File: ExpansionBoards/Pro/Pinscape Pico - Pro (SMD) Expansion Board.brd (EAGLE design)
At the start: 170.6 x 108 mm, 213 parts, among them IC1 UCC27523D, IC10 UCC27523D, IC11 UCC27523D, IC12 UCC27523D, IC13 UCC27523D, IC14 UCC27523D, IC15 TLC59116FIRHBR, IC16 TLC59116FIRHBR, IC17 TLC59116FIRHBR, IC18 TLC59116FIRHBR, IC19 ULN2803ADWR, IC2 UCC27523D, IC20 ULN2803ADWR, IC21 ULN2803ADWR, IC22 ULN2803ADWR, IC23 ULN2803ADWR, IC24 SN74HC165PWR, IC25 SN74HC165PWR, IC26 SN74HC165PWR, IC27 SN74HC165PWR, IC28 LIS3DHTR, IC29 SN74LVC1G175DCKR, IC3 UCC27523D, IC30 APX809S-29SA-7, IC31 LTV-827S, IC32 ADS1115IDGSR, IC33 TLV75733PDBVR, IC34 RV-3032-C7, IC4 UCC27523D, IC5 UCC27523D, IC6 UCC27523D, IC7 UCC27523D, IC8 UCC27523D, IC9 UCC27523D, J1 640445-6, J10 1-640456-0, J11 1-640456-0, J12 1-640456-0, J13 640445-5, J14 640445-9, J15 640445-9, J16 640445-9, J2 30316-6002HB, J3 1-640456-0, J4 640456-9, J5 640456-9, J6 640454-2, J7 215079-4, J8 30308-6002HB, J9 1-640456-0, Q1 BUK7K89-100EX, Q10 BUK7K89-100EX, Q11 BUK7K89-100EX, Q12 BUK7K89-100EX, Q13 BUK7K89-100EX, Q14 BUK7K89-100EX, Q15 UMA5NTR, Q16 UMA5NTR, Q17 UMA5NTR, Q18 UMA5NTR, Q19 UMA5NTR, Q2 BUK7K89-100EX, Q20 UMA5NTR, Q21 UMA5NTR, Q22 UMA5NTR, Q23 UMA5NTR, Q24 UMA5NTR, Q25 UMA5NTR, Q26 UMA5NTR, Q27 DSS8110Y-7, Q3 BUK7K89-100EX, Q4 BUK7K89-100EX, Q5 BUK7K89-100EX, Q6 BUK7K89-100EX, Q7 BUK7K89-100EX, Q8 BUK7K89-100EX, Q9 BUK7K89-100EX, SW1 TS-1187A-B-A-B, U1 BAT-HLD-001-THM

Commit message: exp board: pro: change battery holder to top clip type
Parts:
- removed U1: BAT-HLD-001-THM, SamacSys_Parts:BATHLD001THM
- added BATT1: BH-123A-1, SamacSys_Parts:BH-123A-1
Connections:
- net GND: now also BATT1.-; no longer U1.5
- net N$72: now also BATT1.+; no longer U1.1, U1.2, U1.3, U1.4
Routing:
- net N$72: track 105.0 -> 61.0 mm

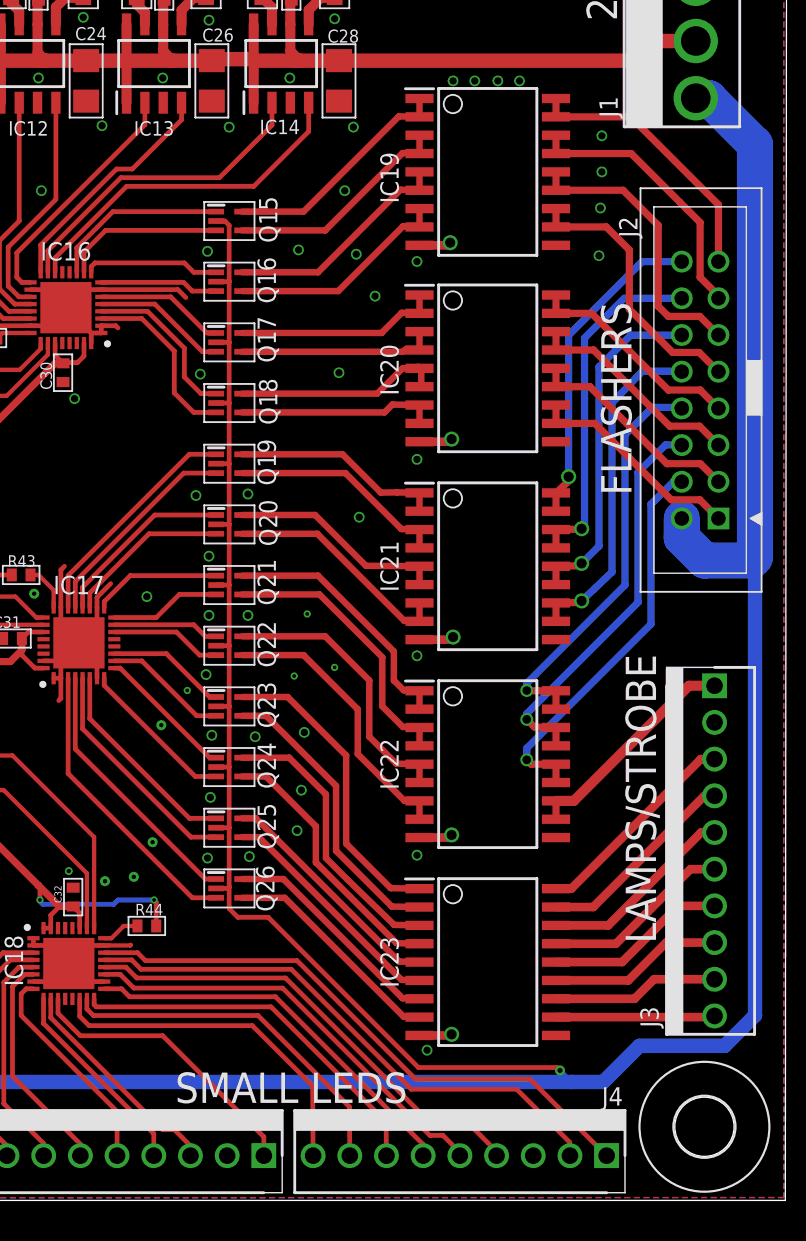
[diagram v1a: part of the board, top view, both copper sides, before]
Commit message: exp board: Pro: change ULN2803ADWR to -CDWR (-ADWR is EOL, replacement is -CDWR)
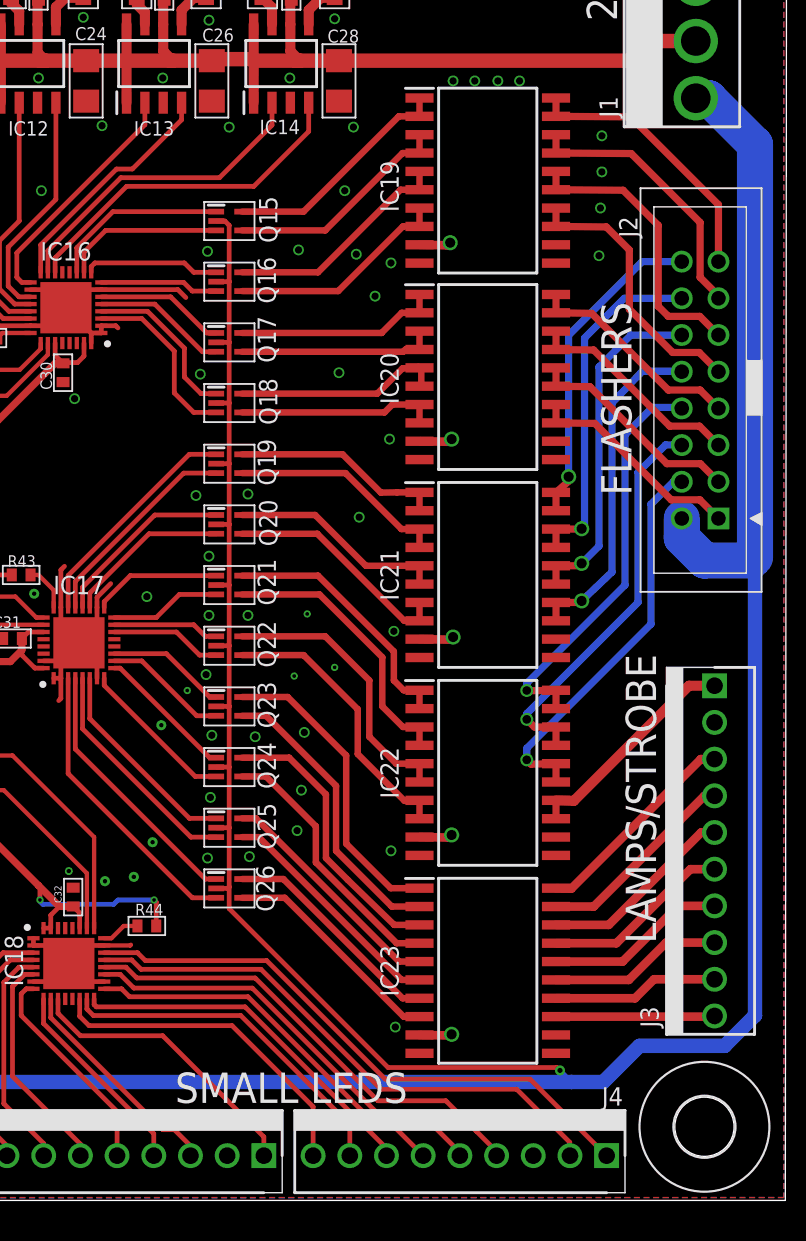
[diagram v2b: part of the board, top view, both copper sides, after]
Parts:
- IC19, IC20, IC21, IC22, IC23: value ULN2803ADWR -> ULN2803CDWR; device SamacSys_Parts:SOIC127P1030X265-18N -> SamacSys_Parts:SOIC127P1030X265-20N
- moved IC19 0.60 mm to (142.9, 69.6)
- moved IC20 0.60 mm to (142.9, 56.0)
- moved IC21 0.60 mm to (142.9, 42.3)
- moved IC23 0.60 mm to (142.9, 14.9)
- moved IC22 0.60 mm to (142.9, 28.6)
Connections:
- net FLASHER1: now also IC19.19, IC19.20; no longer IC19.17, IC19.18
- net FLASHER10: now also IC21.17, IC21.18; no longer IC21.15, IC21.16
- net FLASHER11: now also IC21.15, IC21.16; no longer IC21.13, IC21.14
- net FLASHER12: now also IC21.13, IC21.14; no longer IC21.11, IC21.12
- net FLASHER13: now also IC22.19, IC22.20; no longer IC22.17, IC22.18
- net FLASHER14: now also IC22.17, IC22.18; no longer IC22.15, IC22.16
- net FLASHER15: now also IC22.15, IC22.16; no longer IC22.13, IC22.14
- net FLASHER16: now also IC22.13, IC22.14; no longer IC22.11, IC22.12
- net FLASHER2: now also IC19.17, IC19.18; no longer IC19.15, IC19.16
- net FLASHER3: now also IC19.15, IC19.16; no longer IC19.13, IC19.14
- net FLASHER4: now also IC19.13, IC19.14; no longer IC19.11, IC19.12
- net FLASHER5: now also IC20.19, IC20.20; no longer IC20.17, IC20.18
- net FLASHER6: now also IC20.17, IC20.18; no longer IC20.15, IC20.16
- net FLASHER7: now also IC20.15, IC20.16; no longer IC20.13, IC20.14
- net FLASHER8: now also IC20.13, IC20.14; no longer IC20.11, IC20.12
- net FLASHER9: now also IC21.19, IC21.20; no longer IC21.17, IC21.18
- net LAMP1: now also IC23.20; no longer IC23.18
- net LAMP2: now also IC23.19; no longer IC23.17
- net LAMP3: now also IC23.18; no longer IC23.16
- net LAMP4: now also IC23.17; no longer IC23.15
- net LAMP5: now also IC23.16; no longer IC23.14
- net LAMP6: now also IC23.15; no longer IC23.13
- net LAMP7: now also IC23.14; no longer IC23.12
- net LAMP8: now also IC23.13; no longer IC23.11
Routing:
- net LED6: track 26.3 -> 25.3 mm
- net LED8: track 24.2 -> 23.3 mm
- net LED7: track 25.1 -> 24.4 mm
